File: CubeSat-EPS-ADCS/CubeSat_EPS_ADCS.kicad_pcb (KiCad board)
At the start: 2 copper layers, 92 x 92 mm, 22 parts, among them J1 Conn_01x02_Pin, J2 Conn_01x03_Pin, J3 Conn_01x08_Pin, J4 Screw_Terminal_01x02, J5 Screw_Terminal_01x02, J6 Screw_Terminal_01x02, J7 Screw_Terminal_01x02, J8 Screw_Terminal_01x02, U1 DRV8833 Module, U2 DRV8833 Module, U3 Buck_XL4015, U4 Buck_LM2596

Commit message: safety size change
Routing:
- net VCC_5V: track 18.2 -> 19.1 mm
- net VCC_8.4V_ADCS: track 67.2 -> 68.1 mm
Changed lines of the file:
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@@
+	)
+	(segment
+		(start 17 -48.5)
+		(end 17 -13.56)
+		(width 3)
+		(layer "B.Cu")
+		(net 12)
+	)
+	(segment
+		(start 36.34 -7.48)
+		(end 40.91 -2.91)
+		(width 3)
+		(layer "B.Cu")
+		(net 12)
+	)
+	(segment
+		(start 75.48 -48.46)
+		(end 80.25 -48.46)
+		(width 2)
+		(layer "B.Cu")
+		(net 12)
+	)
+	(segment
+		(start 65.85 -7.83)
+		(end 65.85 -11.82)
+		(width 3)
+		(layer "B.Cu")
+		(net 12)
+	)
+	(segment
+		(start 66.5 -58.5)
+		(end 40.38 -58.5)
+		(width 2)
+		(layer "B.Cu")
+		(net 12)
+	)
+	(segment
+		(start 80.25 -48.46)
+		(end 80.52 -48.73)
+		(width 1)
+		(layer "B.Cu")
+		(net 12)
+	)
+	(segment
+		(start 81.13 -60.05)
+		(end 74.04 -60.05)
+		(width 2)
+		(layer "B.Cu")
+		(net 12)
+	)
+	(segment
+		(start 71.57 -68.26)
+		(end 78.31 -75)
+		(width 2)
+		(layer "B.Cu")
+		(net 12)
+	)
+	(segment
+		(start 88.27 -14.35)
+		(end 88.27 -26.7)
+		(width 2)
+		(layer "B.Cu")
+		(net 12)
+	)
+	(segment
+		(start 69.66 -42.64)
+		(end 69.66 -20.12)
+		(width 2)
+		(layer "B.Cu")
+		(net 12)
+	)
+	(segment
+		(start 90.75 -47.5)
+		(end 90.75 -42.75)
+		(width 1)
+		(layer "B.Cu")
+		(net 12)
+	)
+	(segment
+		(start 89.4 -41.4)
+		(end 88 -41.4)
+		(width 1)
+		(layer "B.Cu")
+		(net 12)
+	)
+	(segment
+		(start 89.35 -48.9)
+		(end 90.75 -47.5)
+		(width 1)
+		(layer "B.Cu")
+		(net 12)
+	)
+	(segment
+		(start 65.85 -11.82)
+		(end 65.85 -9.98)
+		(width 2)
+		(layer "B.Cu")
+		(net 12)
+	)
+	(segment
+		(start 69.66 -20.12)
+		(end 65.85 -16.31)
+		(width 2)
+		(layer "B.Cu")
+		(net 12)
+	)
+	(segment
+		(start 88 -62)
+		(end 86.08 -60.08)
+		(width 2)
+		(layer "B.Cu")
+		(net 12)
+	)
+	(segment
+		(start 71.57 -62.52)
+		(end 71.57 -68.26)
+		(width 2)
+		(layer "B.Cu")
+		(net 12)
+	)
+	(segment
+		(start 75.51 -72.35)
+		(end 38.52 -72.35)
+		(width 2)
+		(layer "B.Cu")
+		(net 12)
+	)
+	(segment
+		(start 80.52 -48.73)
+		(end 87.83 -48.73)
+		(width 1)
+		(layer "B.Cu")
+		(net 12)
 	)
 	(segment
@@
 	)
 	(segment
-		(start 17 -48.5)
-		(end 17 -13.56)
-		(width 3)
-		(layer "B.Cu")
-		(net 12)
-	)
-	(segment
-		(start 36.34 -7.48)
-		(end 40.91 -2.91)
-		(width 3)
-		(layer "B.Cu")
-		(net 12)
-	)
-	(segment
-		(start 75.48 -48.46)
-		(end 80.25 -48.46)
-		(width 2)
-		(layer "B.Cu")
-		(net 12)
-	)
-	(segment
-		(start 65.85 -7.83)
-		(end 65.85 -11.82)
-		(width 3)
-		(layer "B.Cu")
-		(net 12)
-	)
-	(segment
-		(start 88 -62)
-		(end 86.08 -60.08)
-		(width 2)
-		(layer "B.Cu")
-		(net 12)
-	)
-	(segment
-		(start 66.5 -58.5)
-		(end 40.38 -58.5)
-		(width 2)
-		(layer "B.Cu")
-		(net 12)
-	)
-	(segment
-		(start 80.25 -48.46)
-		(end 80.52 -48.73)
-		(width 1)
-		(layer "B.Cu")
-		(net 12)
-	)
-	(segment
-		(start 81.13 -60.05)
-		(end 74.04 -60.05)
-		(width 2)
-		(layer "B.Cu")
-		(net 12)
-	)
-	(segment
-		(start 71.57 -68.26)
-		(end 78.31 -75)
-		(width 2)
-		(layer "B.Cu")
-		(net 12)
-	)
-	(segment
-		(start 88.27 -14.35)
-		(end 88.27 -26.7)
-		(width 2)
-		(layer "B.Cu")
-		(net 12)
-	)
-	(segment
-		(start 69.66 -42.64)
-		(end 69.66 -20.12)
-		(width 2)
-		(layer "B.Cu")
-		(net 12)
-	)
-	(segment
-		(start 90.75 -47.5)
-		(end 90.75 -42.75)
-		(width 1)
-		(layer "B.Cu")
-		(net 12)
-	)
-	(segment
-		(start 89.4 -41.4)
-		(end 88 -41.4)
-		(width 1)
-		(layer "B.Cu")
-		(net 12)
-	)
-	(segment
-		(start 89.35 -48.9)
-		(end 90.75 -47.5)
-		(width 1)
-		(layer "B.Cu")
-		(net 12)
-	)
-	(segment
-		(start 65.85 -11.82)
-		(end 65.85 -9.98)
-		(width 2)
-		(layer "B.Cu")
-		(net 12)
-	)
-	(segment
-		(start 69.66 -20.12)
-		(end 65.85 -16.31)
-		(width 2)
-		(layer "B.Cu")
-		(net 12)
-	)
-	(segment
-		(start 71.57 -62.52)
-		(end 71.57 -68.26)
-		(width 2)
-		(layer "B.Cu")
-		(net 12)
-	)
-	(segment
-		(start 75.51 -72.35)
-		(end 38.52 -72.35)
-		(width 2)
-		(layer "B.Cu")
-		(net 12)
-	)
-	(segment
-		(start 80.52 -48.73)
-		(end 87.83 -48.73)
-		(width 1)
-		(layer "B.Cu")
-		(net 12)
-	)
-	(segment
 		(start 88 -48.9)
 		(end 89.35 -48.9)
@@
 	)
 	(segment
+		(start 90.75 -42.75)
+		(end 89.4 -41.4)
+		(width 1)
+		(layer "B.Cu")
+		(net 12)
+	)
+	(segment
+		(start 88.27 -26.7)
+		(end 85.41 -29.56)
+		(width 2)
+		(layer "B.Cu")
+		(net 12)
+	)
+	(segment
+		(start 40.91 -2.91)
+		(end 60.93 -2.91)
+		(width 3)
+		(layer "B.Cu")
+		(net 12)
+	)
+	(segment
+		(start 79.01 -5.09)
+		(end 88.27 -14.35)
+		(width 2)
+		(layer "B.Cu")
+		(net 12)
+	)
+	(segment
+		(start 23.04 -54.54)
+		(end 17 -48.5)
+		(width 3)
+		(layer "B.Cu")
+		(net 12)
+	)
+	(segment
 		(start 81.16 -60.08)
 		(end 81.13 -60.05)
@@
 	)
 	(segment
-		(start 90.75 -42.75)
-		(end 89.4 -41.4)
-		(width 1)
-		(layer "B.Cu")
-		(net 12)
-	)
-	(segment
-		(start 88.27 -26.7)
-		(end 85.41 -29.56)
-		(width 2)
-		(layer "B.Cu")
-		(net 12)
-	)
-	(segment
-		(start 40.91 -2.91)
-		(end 60.93 -2.91)
-		(width 3)
-		(layer "B.Cu")
-		(net 12)
-	)
-	(segment
-		(start 79.01 -5.09)
-		(end 88.27 -14.35)
-		(width 2)
-		(layer "B.Cu")
-		(net 12)
-	)
-	(segment
-		(start 23.04 -54.54)
-		(end 17 -48.5)
-		(width 3)
-		(layer "B.Cu")
-		(net 12)
-	)
-	(segment
 		(start 80.5 -51.25)
 		(end 80.25 -51)
@@
 	)
 	(segment
-		(start 81.13 -69.66)
-		(end 86.29 -64.5)
+		(start 81.13 -70.21)
+		(end 81.13 -68.12)
 		(width 2)
 		(layer "B.Cu")
@@
 	)
 	(segment
+		(start 84.75 -64.5)
+		(end 88 -64.5)
+		(width 2)
+		(layer "B.Cu")
+		(net 22)
+	)
+	(segment
 		(start 75.91 -63.89)
 		(end 75.91 -63.95)
@@
 	)
 	(segment
-		(start 86.29 -64.5)
-		(end 88 -64.5)
-		(width 2)
-		(layer "B.Cu")
-		(net 22)
-	)
-	(segment
-		(start 81.13 -70.21)
-		(end 81.13 -69.66)
+		(start 81.13 -68.12)
+		(end 84.75 -64.5)
 		(width 2)
 		(layer "B.Cu")
@@
 	)
 	(segment
-		(start 84.12 -24.79)
-		(end 81.89 -27.02)
-		(width 2)
-		(layer "B.Cu")
-		(net 25)
-	)
-	(segment
-		(start 84.12 -16.66)
-		(end 84.12 -24.79)
+		(start 70.85 -11.82)
+		(end 79.28 -11.82)
 		(width 2)
 		(layer "B.Cu")
@@
 	)
 	(segment
-		(start 81.89 -27.02)
-		(end 80.41 -27.02)
-		(width 2)
-		(layer "B.Cu")
-		(net 25)
-	)
-	(segment
-		(start 79.28 -11.82)
-		(end 84.12 -16.66)
-		(width 2)
-		(layer "B.Cu")
-		(net 25)
-	)
-	(segment
 		(start 70.85 -12.01)
 		(end 70.85 -11.82)
@@
 	)
 	(segment
+		(start 79.28 -11.82)
+		(end 84.75 -17.29)
+		(width 2)
+		(layer "B.Cu")
+		(net 25)
+	)
+	(segment
+		(start 84.75 -17.29)
+		(end 84.75 -24.75)
+		(width 2)
+		(layer "B.Cu")
+		(net 25)
+	)
+	(segment
+		(start 84.75 -24.75)
+		(end 82.48 -27.02)
+		(width 2)
+		(layer "B.Cu")
+		(net 25)
+	)
+	(segment
 		(start 74.94 -42.63)
 		(end 74.94 -16.1)
@@
 	)
 	(segment
-		(start 70.85 -11.82)
-		(end 79.28 -11.82)
-		(width 2)
-		(layer "B.Cu")
+		(start 82.48 -27.02)
+		(end 80.41 -27.02)
+		(width 2)
+		(layer "B.Cu")

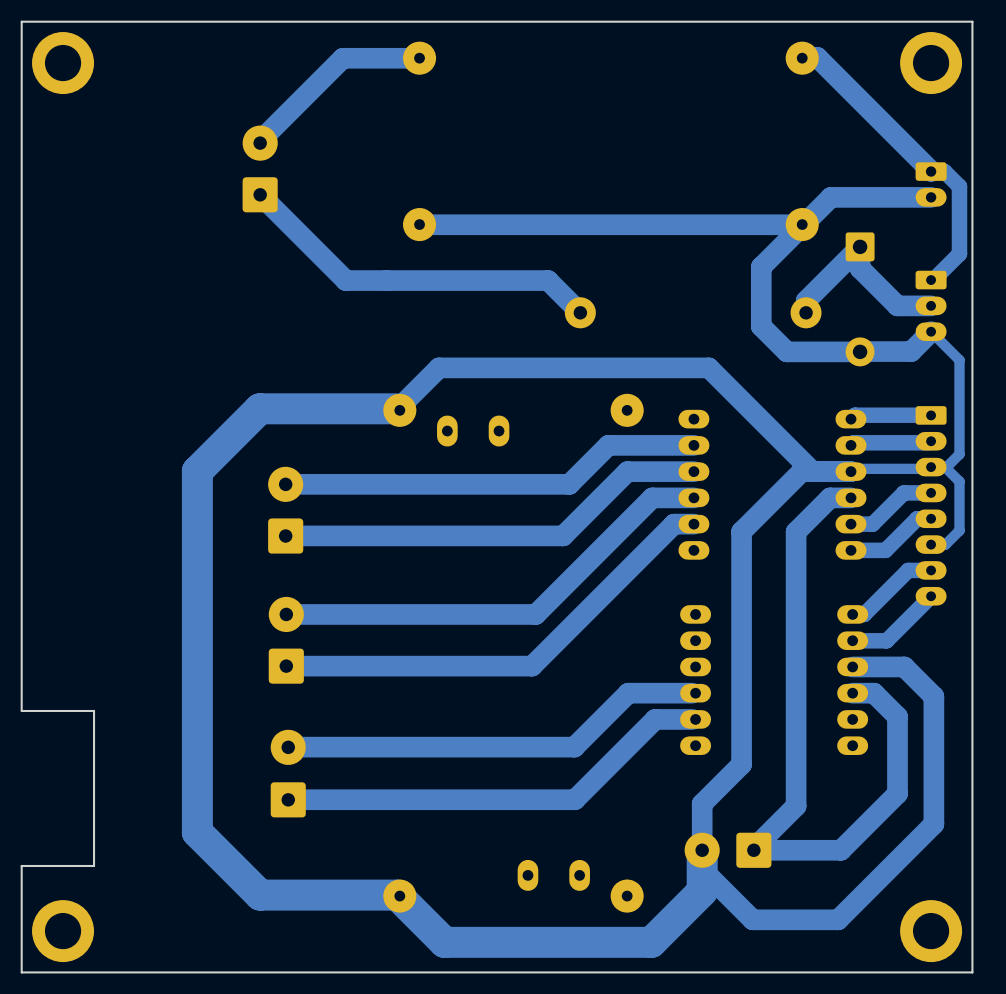
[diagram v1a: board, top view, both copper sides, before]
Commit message: new Main and EPS PCBs, all previous problems corrected, final version
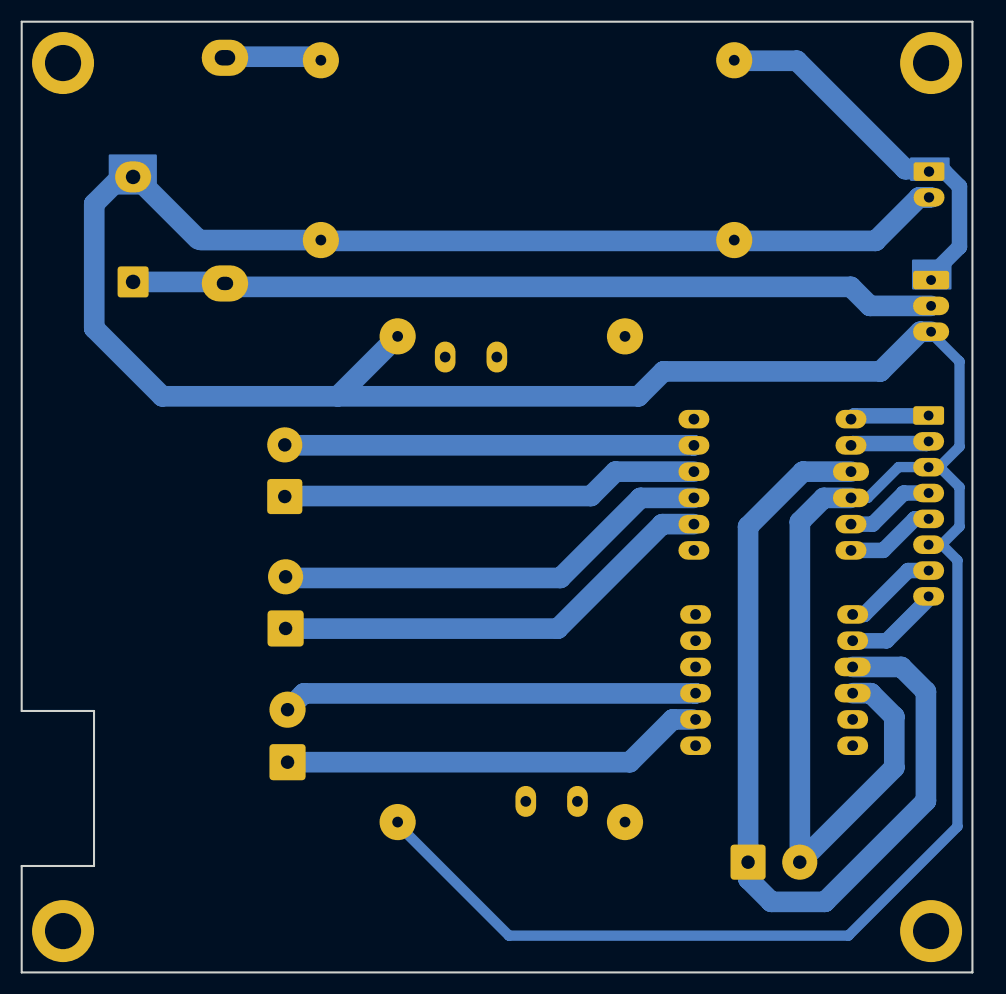
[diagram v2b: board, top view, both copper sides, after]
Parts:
- removed the G*** at (27.3, -3.34)
- removed the G*** at (26.3, -88.0)
- removed J8: Screw_Terminal_01x02, TerminalBlock_Phoenix:TerminalBlock_Phoenix_MKDS-1,5-2_1x02_P5.00mm_Horizontal
- added G***: LOGO, Logos:EPS_Symbol2, B.Cu at (79.7, -65.0)
- added G***: LOGO, Logos:EPS_Symbol2, B.Cu at (28.6, -60.5)
- moved D1 70.4 mm to (10.8, -66.8), turned to 90 degrees
- moved G*** 68.2 mm to (22.0, -4.27), turned to 180 degrees
- moved F1 47.4 mm to (19.7, -77.6), turned to -90 degrees
- moved G*** 47.0 mm to (3.82, -81.4), turned to -90 degrees
- moved U4 7.92 mm to (49.0, -79.6)
- moved U3 7.16 mm to (47.4, -38.0)
- moved J5 3.82 mm to (25.5, -46.0)
- moved J7 3.65 mm to (25.7, -20.3)
- moved J6 3.65 mm to (25.5, -33.3)
- moved J4 1.28 mm to (70.3, -10.7), turned to 0 degrees
- moved J3 0.24 mm to (87.8, -53.9)
- moved J1 0.20 mm to (87.8, -77.5)
- renumbered J6 to J5, J5 to J6
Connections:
- F1 pad 1: Net-(J8-Pin_1) -> Net-(U4-Vout)
- U1 pad 10: GND -> VCC_8.4V_ADCS
- U1 pad 9: VCC_8.4V_ADCS -> GND
- U2 pad 10: GND -> VCC_8.4V_ADCS
- U2 pad 9: VCC_8.4V_ADCS -> GND
- U4 pad 3: Net-(J8-Pin_2) -> Net-(U4-Vout)
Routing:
- net VCC_5V: track 19.1 -> 78.2 mm
- net Net-(J8-Pin_1): track 35.7 -> 0.00 mm
- net Net-(J8-Pin_2): track 18.9 -> 0.00 mm
- net VCC_8.4V_ADCS: track 68.1 -> 87.0 mm
- net Net-(U4-Vout): track 0.00 -> 9.46 mm
- net VCC_8.4V_EPS: track 30.8 -> 37.1 mm
- net GND: track 378.2 -> 384.3 mm
- net VCC_M2: track 42.1 -> 40.6 mm
- net GND_M2: track 41.1 -> 39.6 mm
- net VCC_M3: track 42.3 -> 40.9 mm
- net GND_M1: track 44.1 -> 42.8 mm
- net GND_M3: track 41.3 -> 40.2 mm
- net VCC_M1: track 44.8 -> 43.8 mm
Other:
- board text added: "EPS/ADCS"
- board text added: "Main Power Suply"
- board text added: "Motor Control"
- board text added: "Vdrv"
- board text removed: "5V | 1A"
- board text removed: "ADCS"
- board text removed: "ON/OFF SWITCH"

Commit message: small changes in layout
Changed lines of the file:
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@@
 	(footprint "TerminalBlock_Phoenix:TerminalBlock_Phoenix_MKDS-1,5-2_1x02_P5.00mm_Horizontal"
 		(layer "B.Cu")
-		(at 25.5375 -33.285 90)
+		(at 25.5375 -33.2625 90)
 		(descr "Terminal Block Phoenix MKDS-1,5-2, 2 pins, pitch 5mm, size 10x9.8mm, drill diameter 1.3mm, pad diameter 2.6mm, http://www.farnell.com/datasheets/100425.pdf, script-generated using https://gitlab.com/kicad/libraries/kicad-footprint-generator/-/tree/master/scripts/TerminalBlock_Phoenix")
 		(tags "THT Terminal Block Phoenix MKDS-1,5-2 pitch 5mm size 10x9.8mm drill 1.3mm pad 2.6mm")

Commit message: minor changes in the design
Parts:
- ? (x4), D1, F1, G*** (x4), J1, J2, J3, J4, J5, J6, J7, U1, U2, U3, U4: moved to F.Cu
- moved G*** 84.4 mm to (88.2, -81.4)
- moved ? 84.0 mm to (4.00, -4.00), turned to 0 degrees
- moved ? 84.0 mm to (88.0, -88.0), turned to 0 degrees
- moved ? 84.0 mm to (4.00, -88.0), turned to 0 degrees
- moved ? 84.0 mm to (88.0, -4.00), turned to 0 degrees
- moved J2 84.0 mm to (4.00, -67.0)
- moved J1 83.6 mm to (4.20, -77.5)
- moved J3 83.5 mm to (4.24, -53.9)
- moved D1 70.4 mm to (81.2, -66.8)
- moved G*** 67.4 mm to (12.3, -65.0), turned to 0 degrees
- moved U2 53.6 mm to (19.2, -28.3), turned to 180 degrees
- moved U1 53.3 mm to (19.4, -47.2), turned to 180 degrees
- moved F1 52.7 mm to (72.3, -77.6)
- moved J4 48.6 mm to (21.7, -10.7), turned to 180 degrees
- moved G*** 48.0 mm to (70.0, -4.27), turned to 0 degrees
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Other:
- outline, holes or cut-outs redrawn
